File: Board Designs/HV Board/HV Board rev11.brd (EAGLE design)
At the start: 118.6 x 71.4 mm, 62 parts, among them IC1 OKI-78SR-5, IC2 NE5532SOIC

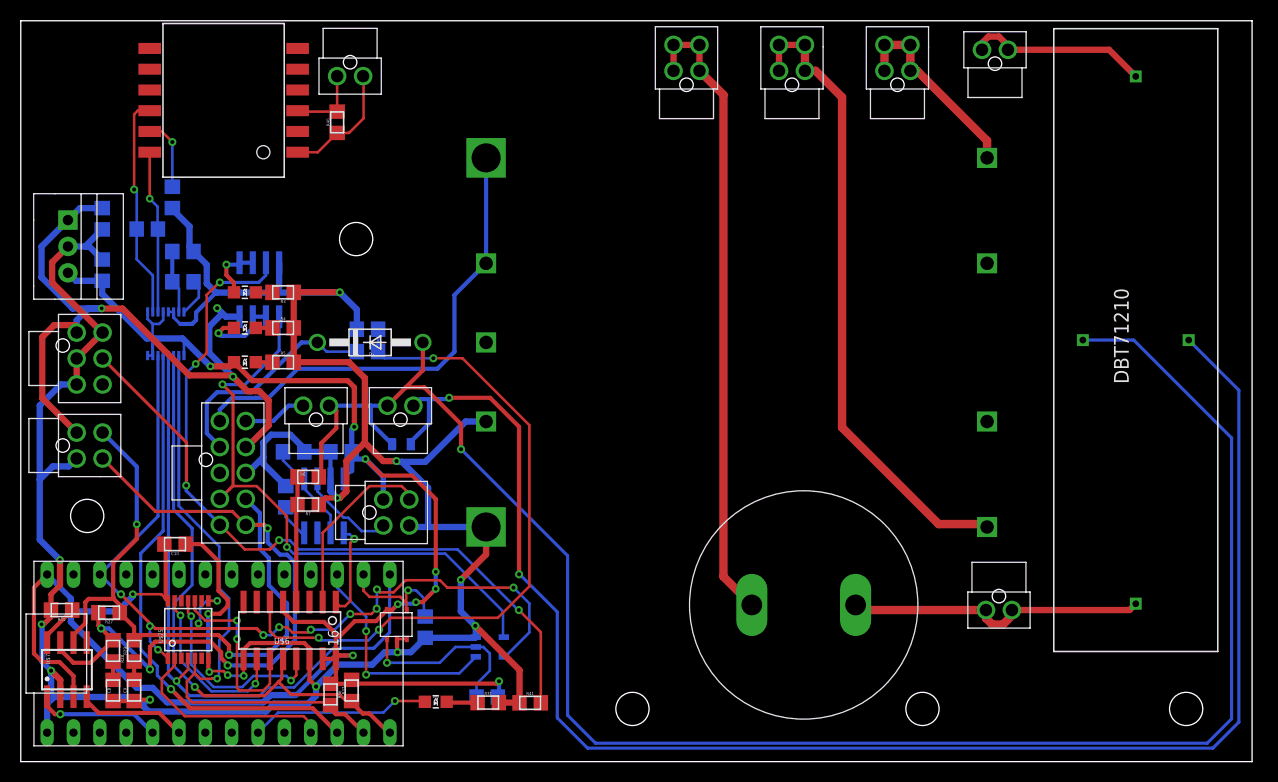
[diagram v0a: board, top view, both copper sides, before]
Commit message: HV Board rev11: Update discharge relay holes and pads, change ADC to read shutdown_G, moved silkscreen
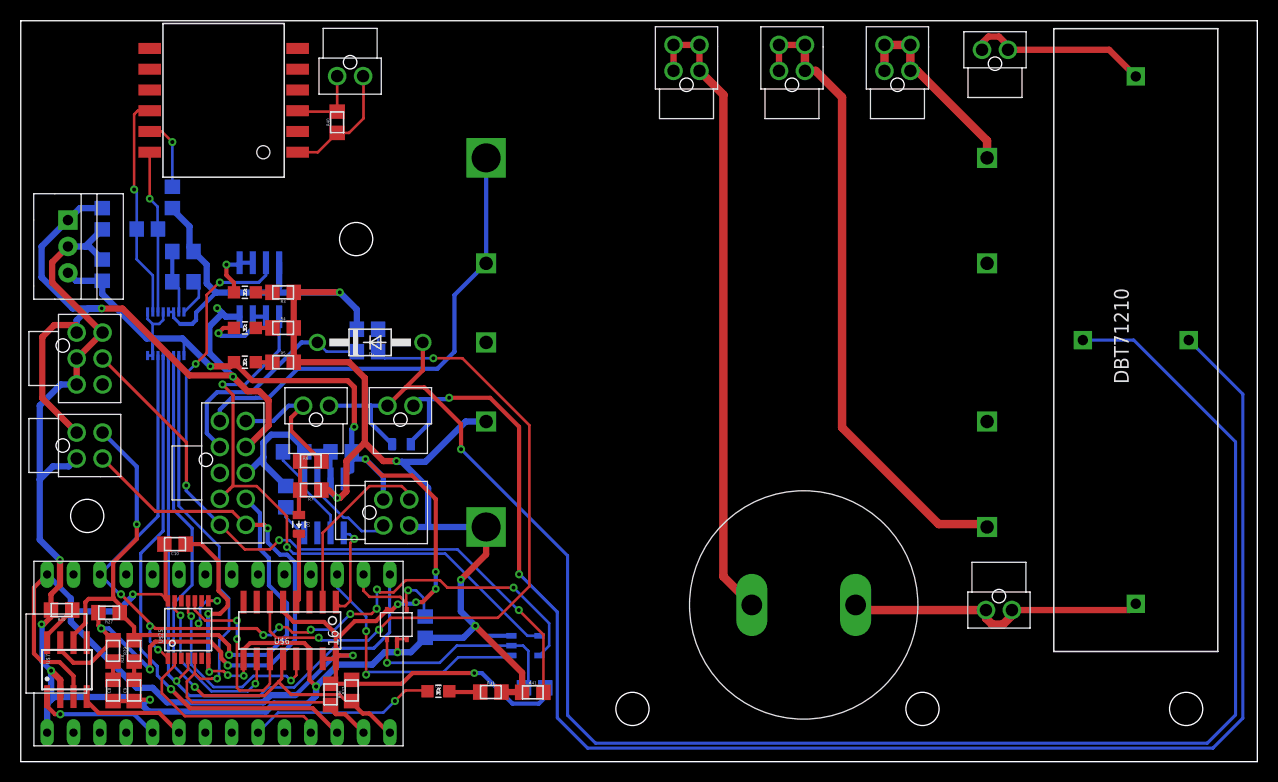
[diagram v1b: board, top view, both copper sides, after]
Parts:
- added D3: TS4148 RYG, HyTechDevices:0805_D
- moved R38 4.66 mm to (49.5, 7.11)
- moved U$3 3.43 mm to (48.6, 11.2)
- moved R6 1.55 mm to (27.9, 29.0)
- moved R7 1.42 mm to (27.9, 26.2)
- moved LED 1.05 mm to (40.2, 6.78)
- moved R31 1.05 mm to (45.3, 6.71)
- moved R41 1.05 mm to (49.3, 6.68)
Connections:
- net SHUTDOWN7_EXT_OUT renamed CHARGE_ENABLE
- removed net SHUTDOWN6: INTERLOCK.P$1, MAIN.P$6
- removed net SHUTDOWN7: D1.A, D2.C, INTERLOCK.P$2, R6.1, RELAYS.P$1, U$4.COIL+
- new net N$10: D3.C, U$6.4
- new net SHUTDOWN_G: INTERLOCK.P$1, MAIN.P$6, R6.1
- new net SHUTDOWN_H: D1.A, D2.C, INTERLOCK.P$2, RELAYS.P$1, U$4.COIL+
- net N$9: now also D3.A; no longer U$6.4
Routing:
- net SHUTDOWN7: track 176.1 -> 0.00 mm, vias 1 -> 0
- net SHUTDOWN_H: track 0.00 -> 168.4 mm, vias 0 -> 1
- net SHUTDOWN_G: track 0.00 -> 13.2 mm
- net N$9: track 12.1 -> 5.24 mm
- net N$10: track 0.00 -> 6.70 mm
- net SHUTDOWN6: track 6.13 -> 0.00 mm
- net +5V: track 189.1 -> 194.7 mm
- net N$40: track 22.1 -> 25.6 mm
- net N$38: track 17.8 -> 20.5 mm
- net GND: track 296.9 -> 299.0 mm
- net BMS_OK: track 57.8 -> 59.7 mm
- net OKHS: track 90.4 -> 89.5 mm
- net N$37: track 17.4 -> 18.0 mm
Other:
- board size 118.6 x 71.4 mm -> 119.1 x 71.4 mm
- board text added: "2019 HV_board_rev11 Designed by Yvonne Yeh"
- board text removed: "2019 HV_board_rev10 Designed by Yvonne Yeh"

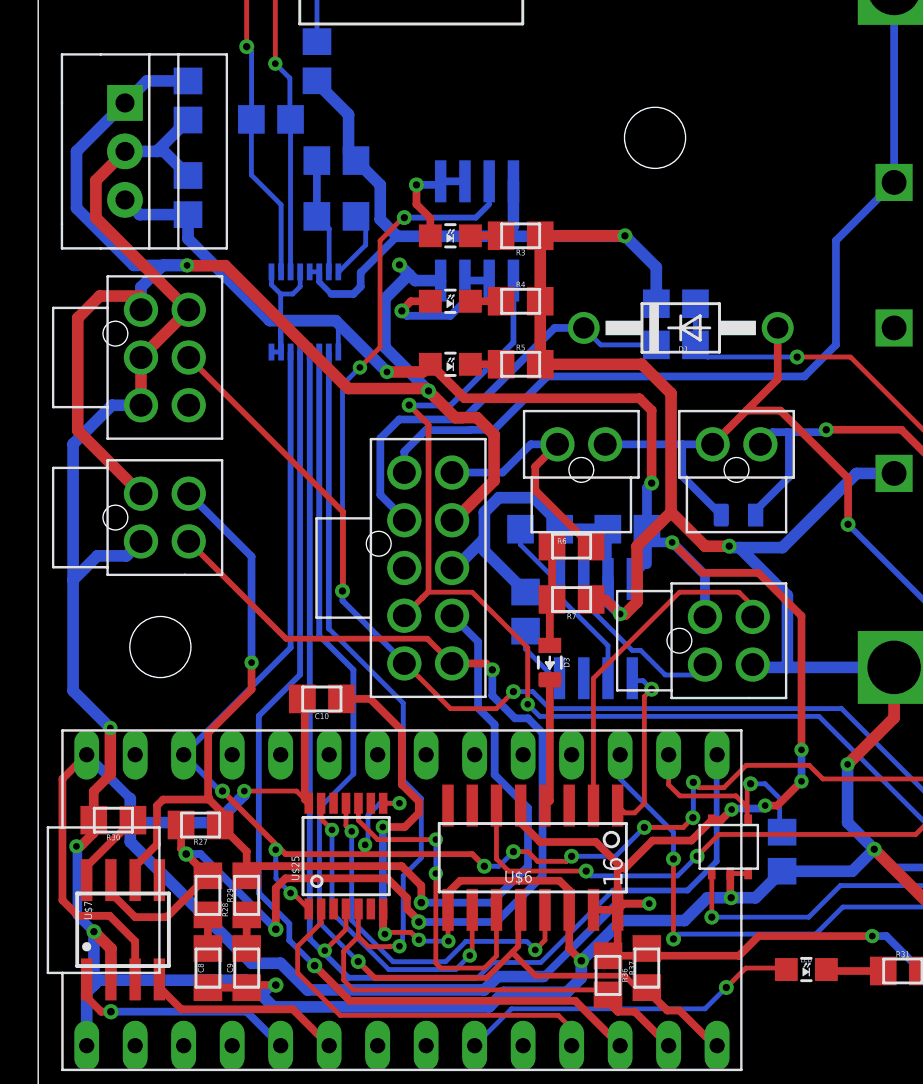
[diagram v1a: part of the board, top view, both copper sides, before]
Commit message: HV Board rev11: Amplified BMS_OK signal, added split CAN termination and TVS diode
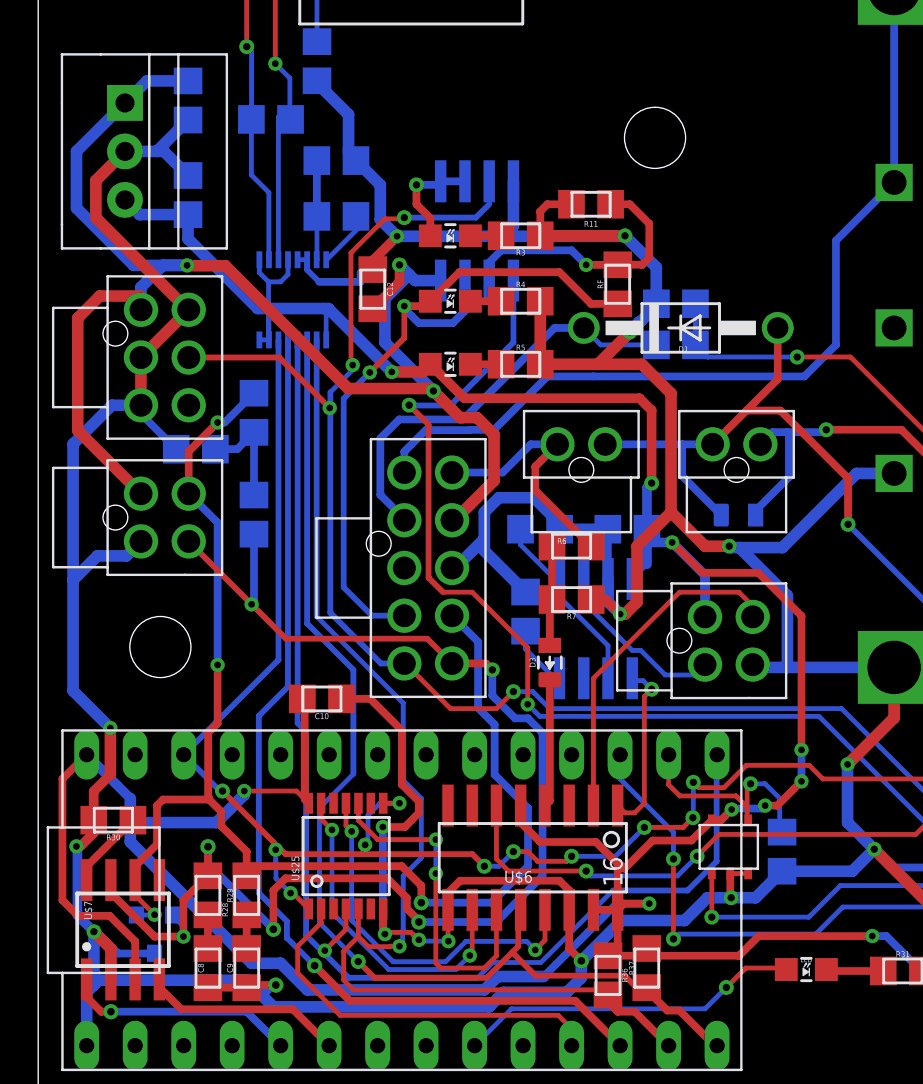
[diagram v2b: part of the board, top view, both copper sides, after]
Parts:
- removed R27: 120, HyTechDevices:0805
- added C11, C12: 0.1uF, HyTechDevices:0805
- added R11: 1k, HyTechDevices:0805
- added R8, R9: 60, HyTechDevices:0805
- added RF: 2k, HyTechDevices:0805
- added U$1: CDSOT23-T24CAN-Q, HyTechDevices:SOT23
- R4: value 820 -> 5k
- moved U$8 0.90 mm to (15.0, 40.3)
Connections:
- removed net BMS_OK: IC2.5, MAIN.P$4, U$3.4
- removed net N$43: BMS-OK.A, IC2.6, IC2.7
- new net BMS_OK_10V: BMS-OK.A, IC2.7, MAIN.P$4, RF.2
- new net BMS_OK_3.3V: IC2.5, U$3.4
- new net N$11: C11.2, R8.1, R9.1
- new net N$12: IC2.6, R11.2, RF.1
- net +12V: now also C12.1
- net CANH: now also R8.2, U$1.2; no longer R27.2
- net CANL: now also R9.2, U$1.1; no longer R27.1
- net GND: now also C11.1, C12.2, R11.1, U$1.3
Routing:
- net BMS_OK: track 59.7 -> 0.00 mm, vias 2 -> 0
- net BMS_OK_3.3V: track 0.00 -> 57.1 mm, vias 0 -> 2
- net BMS_OK_10V: track 0.00 -> 37.9 mm, vias 0 -> 2
- net N$12: track 0.00 -> 14.3 mm, vias 0 -> 1
- net GND: track 299.0 -> 312.3 mm, vias 15 -> 17
- net CANL: track 62.5 -> 71.0 mm, vias 2 -> 4
- net N$43: track 7.80 -> 0.00 mm, vias 1 -> 0
- net N$11: track 0.00 -> 5.67 mm
- net OKHS: track 89.5 -> 84.2 mm
- net CANH: track 66.4 -> 71.2 mm, vias 4 -> 6
- net +12V: track 71.8 -> 74.8 mm
- net IM: track 21.4 -> 20.5 mm
- net SCK_TEENSY: track 63.9 -> 64.8 mm
- net MISO: track 58.5 -> 59.4 mm
- net N$32: track 6.14 -> 5.24 mm
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
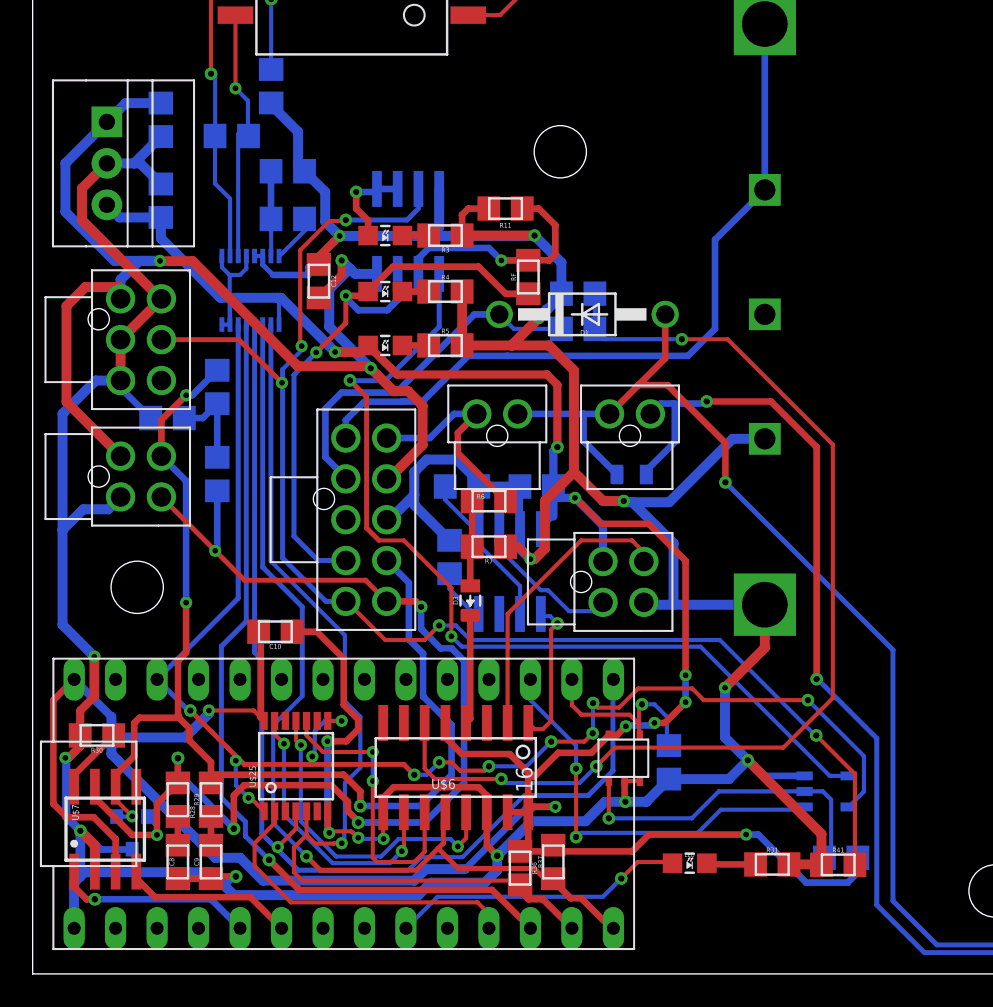
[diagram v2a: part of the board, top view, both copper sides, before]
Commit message: HV Board: Added bypass caps to LTC6820 and SPI level shifter, rerouted under Teensy, rerouted GND/Power to 5V regulator, Silkscreen updates for mfg
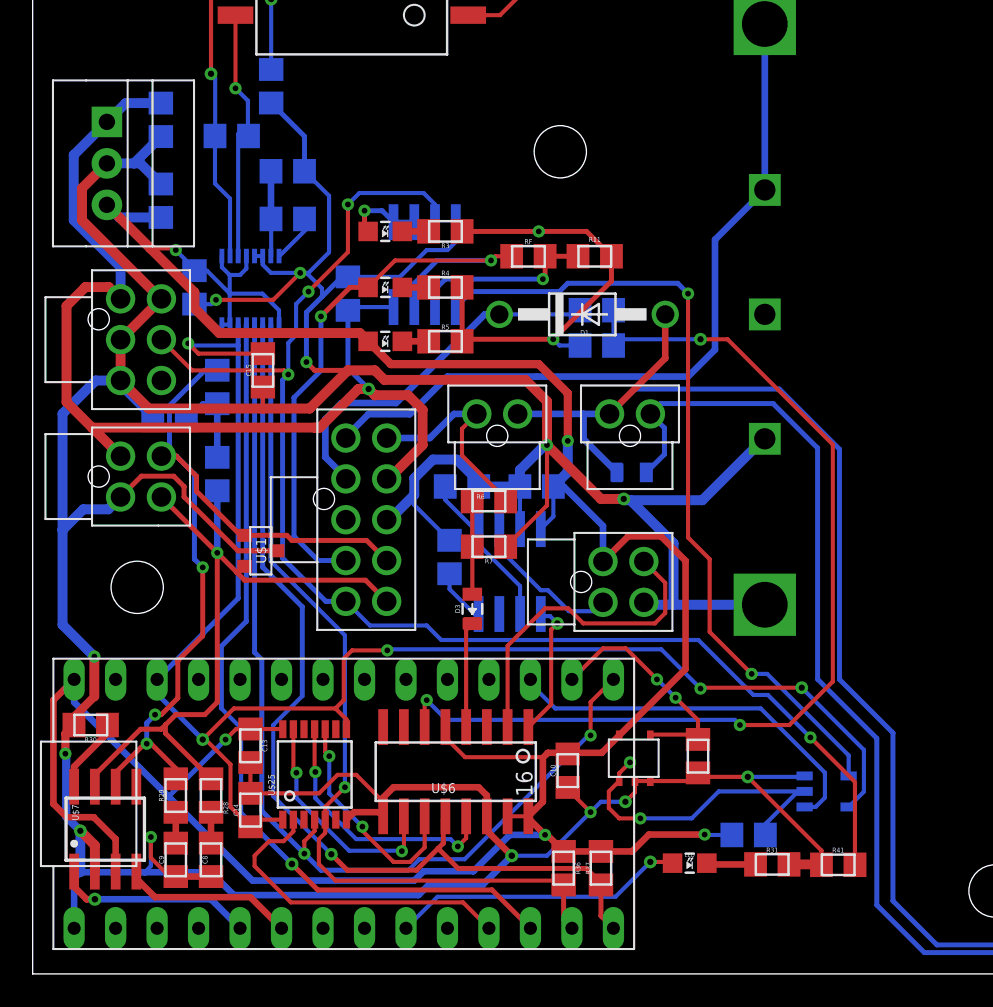
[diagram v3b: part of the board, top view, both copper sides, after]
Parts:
- added C13, C14, C15, C16: 0.1uF, HyTechDevices:0805
- C11: value 0.1uF -> 4.7nF
- moved C10 19.8 mm to (32.8, 12.4), turned to 270 degrees
- moved U$1 19.0 mm to (14.0, 25.9), flipped to the top, turned to 270 degrees
- moved R11 6.19 mm to (34.4, 43.9), turned to 180 degrees
- moved R38 5.83 mm to (43.8, 8.51), turned to 180 degrees
- moved R2 3.37 mm to (34.5, 38.5)
- moved R37 2.95 mm to (34.8, 6.48)
- moved R36 2.67 mm to (32.5, 6.48)
- moved IC2 2.27 mm to (24.0, 43.4)
- moved R29 2.17 mm to (8.76, 10.9)
- moved C9 2.16 mm to (8.76, 6.99)
- moved R28 2.05 mm to (10.9, 10.9)
- moved C8 2.04 mm to (10.9, 6.99)
- moved C12 1.93 mm to (19.3, 41.7), flipped to the bottom
- moved R42 1.82 mm to (40.7, 13.3), flipped to the top
- moved R1 1.62 mm to (34.5, 40.6)
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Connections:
- net +3V3: now also C14.1, C15.2
- net +5V: now also C13.1, C16.2
- net GND: now also C13.2, C14.2, C15.1, C16.1
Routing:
- net GND: track 312.3 -> 345.9 mm, vias 17 -> 15
- net CANH: track 71.2 -> 44.5 mm, vias 6 -> 1
- net CANL: track 71.0 -> 51.5 mm, vias 4 -> 3
- net +5V: track 194.7 -> 179.9 mm, vias 10 -> 5
- net +3V3: track 87.6 -> 97.7 mm, vias 12 -> 5
- net +12V: track 74.8 -> 66.5 mm, vias 3 -> 1
- net BMS_OK_3.3V: track 57.1 -> 49.3 mm
- net SHUTDOWN_H: track 168.4 -> 174.5 mm, vias 1 -> 0
- net MOSI_TEENSY: track 59.6 -> 54.0 mm
- net N$24: track 65.5 -> 61.2 mm
- net MOSI_5V: track 17.8 -> 14.0 mm
- net SCK_5V: track 19.7 -> 16.2 mm
- net SCK_TEENSY: track 64.8 -> 61.4 mm, vias 1 -> 2
- net N$12: track 14.3 -> 11.4 mm
- net N$7: track 17.2 -> 14.3 mm
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
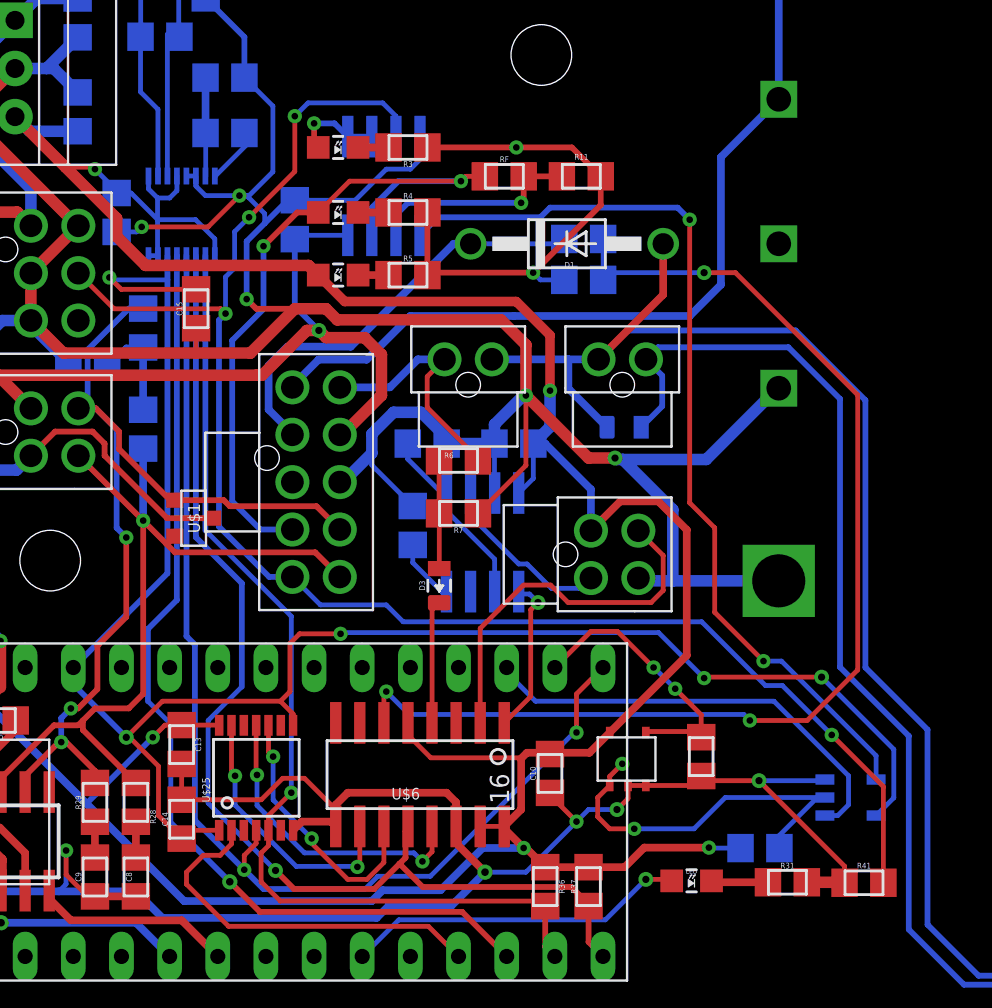
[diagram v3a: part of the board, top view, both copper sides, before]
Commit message: Final version of HV board rev11 sent for mfg
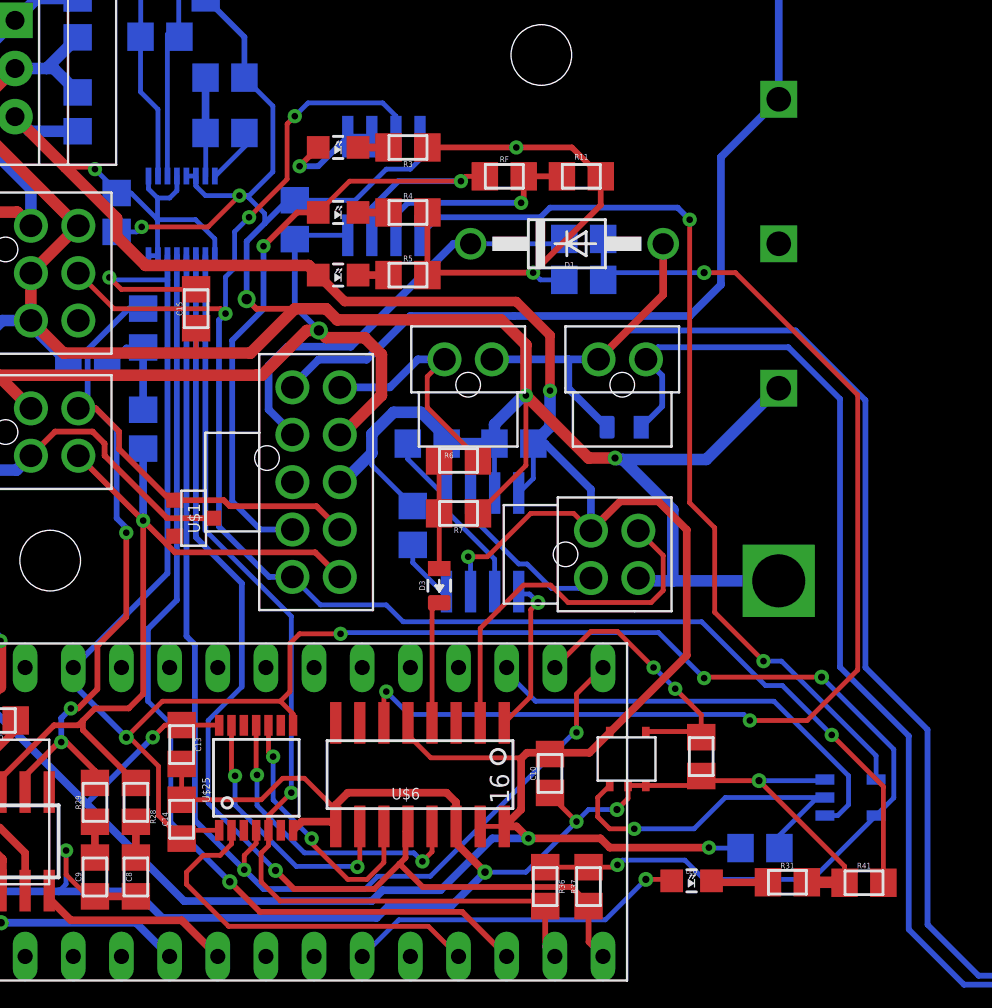
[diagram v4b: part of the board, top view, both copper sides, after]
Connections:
- removed net N$8: U$11.7
- net +3V3: now also R36.1, R37.1
- net +5V: now also U$11.7; no longer R36.1, R37.1
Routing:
- net +3V3: track 97.7 -> 117.1 mm, vias 5 -> 6
- net +5V: track 179.9 -> 189.2 mm, vias 5 -> 6
- net N$38: track 20.2 -> 18.7 mm, vias 2 -> 1
- net N$42: track 4.70 -> 5.85 mm
